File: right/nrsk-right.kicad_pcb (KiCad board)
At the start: 2 copper layers, 199.6 x 132.6 mm, 147 parts, among them J1 PJ-320D, J2 USB-C, J3 OLED 128x32, SW1 71, SW10 8, SW11 9, SW12 0, SW13 -, SW14 =, SW15 Backspace, SW16 75, SW17 Y, SW18 U, SW19 I, SW2 F7, SW20 O, SW21 P, SW22 [, SW23 ], SW24 \, SW25 77, SW26 H, SW27 J, SW28 K, SW29 L, SW3 F8, SW30 ;, SW31 ', SW32 Enter, SW33 79, SW34 N, SW35 M, SW36 ,, SW37 ., SW38 /, SW39 ↑, SW4 F9, SW40 fn, SW41 81, SW42 Space, SW43 Space, SW44 Cmd, SW45 Opt, SW46 ←, SW47 ↓, SW48 →, SW5 F10, SW6 F11, SW7 F12, SW8 73, SW9 7, U1 RP2040, U2 USBLC6-2SC6, U3 AS5600-ASOM, U4 AP2112K-3.3, U5 W25Q128JVS, Y1 12MHz

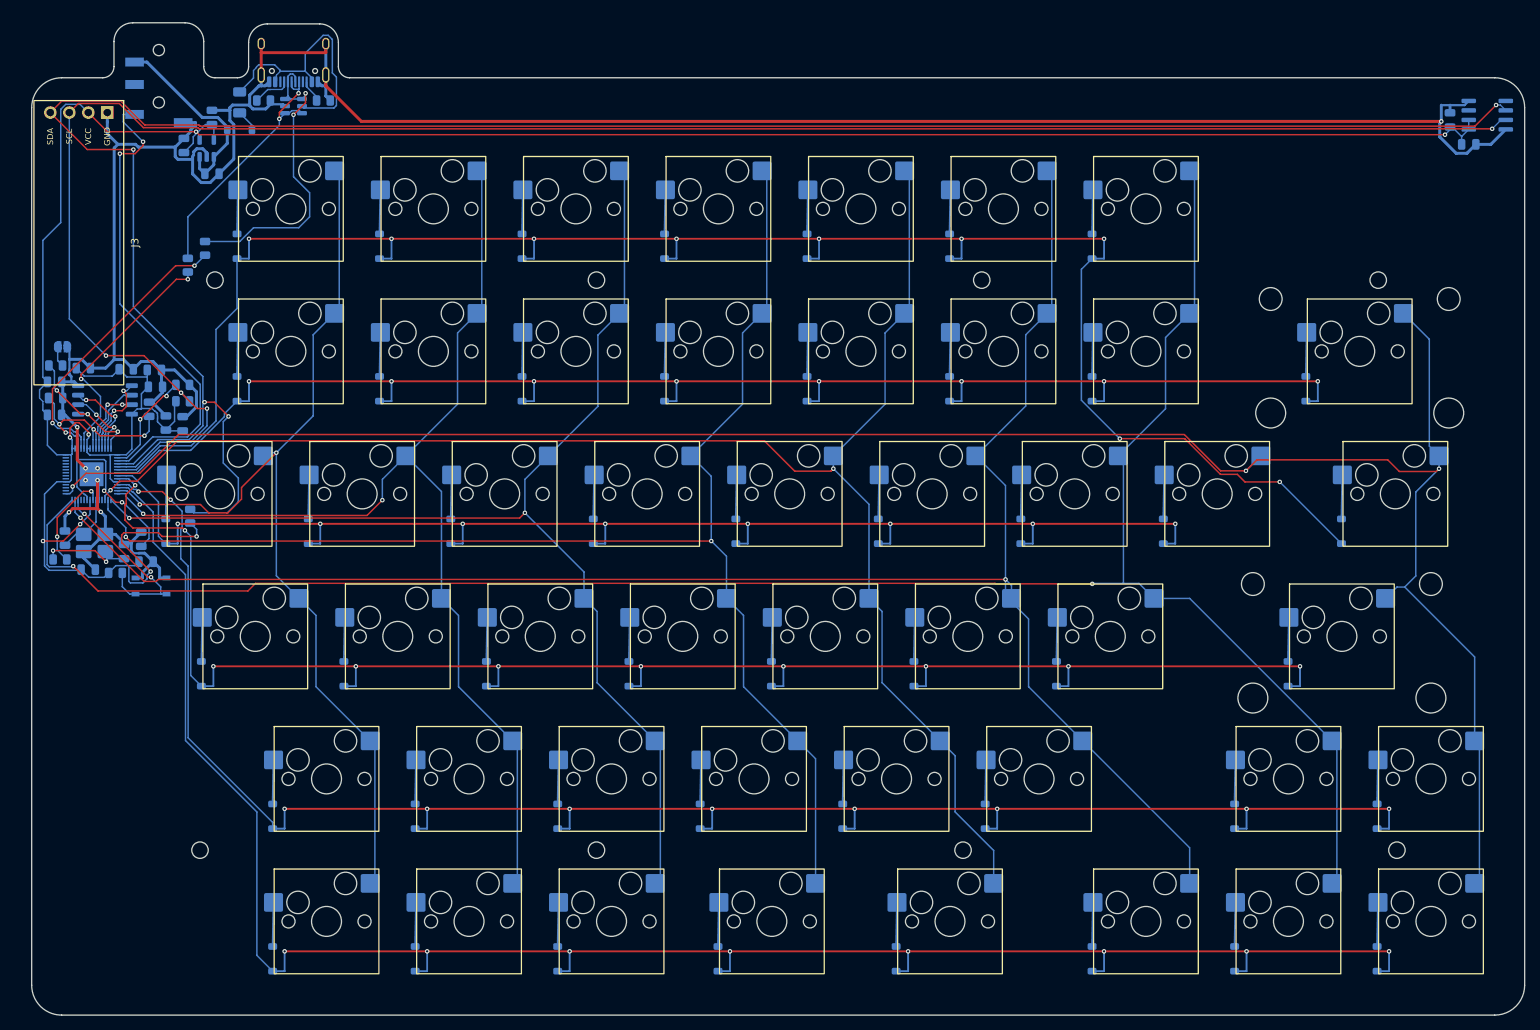
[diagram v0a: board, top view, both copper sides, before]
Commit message: PCB: thumbwheel encoder on the back at the wheel axis, boards re-routed (spec step 3) - ENC1 on the back, rotor on the wheel axis (where U3 was), terminals toward the board inside;   C9 / C10 gone from the support parts - The key turned 180 deg (socket below the stem) is now picked by geometry: a key whose   socket courtyard comes within 0.5 mm of the encoder courtyard. Left: Esc (SW1); right: none - Footprint Datasheet field left empty like the others (it differed from the symbol's) - Re-routed both halves; fab outputs regenerated - Checked: 0 unconnected, 0 DRC errors, 0 footprint errors, 0 schematic parity issues on   both halves (warnings: 5 silk-to-edge on J1/J2 as before, 3 / 2 dangling GND vias);   the gerber Edge.Cuts carries the rotor cut-out (3.1 mm square, lobes to +/-2.3 mm) at both wheel axes
Co-Authored-By: Claude Opus 5.5 <noreply@anthropic.com>
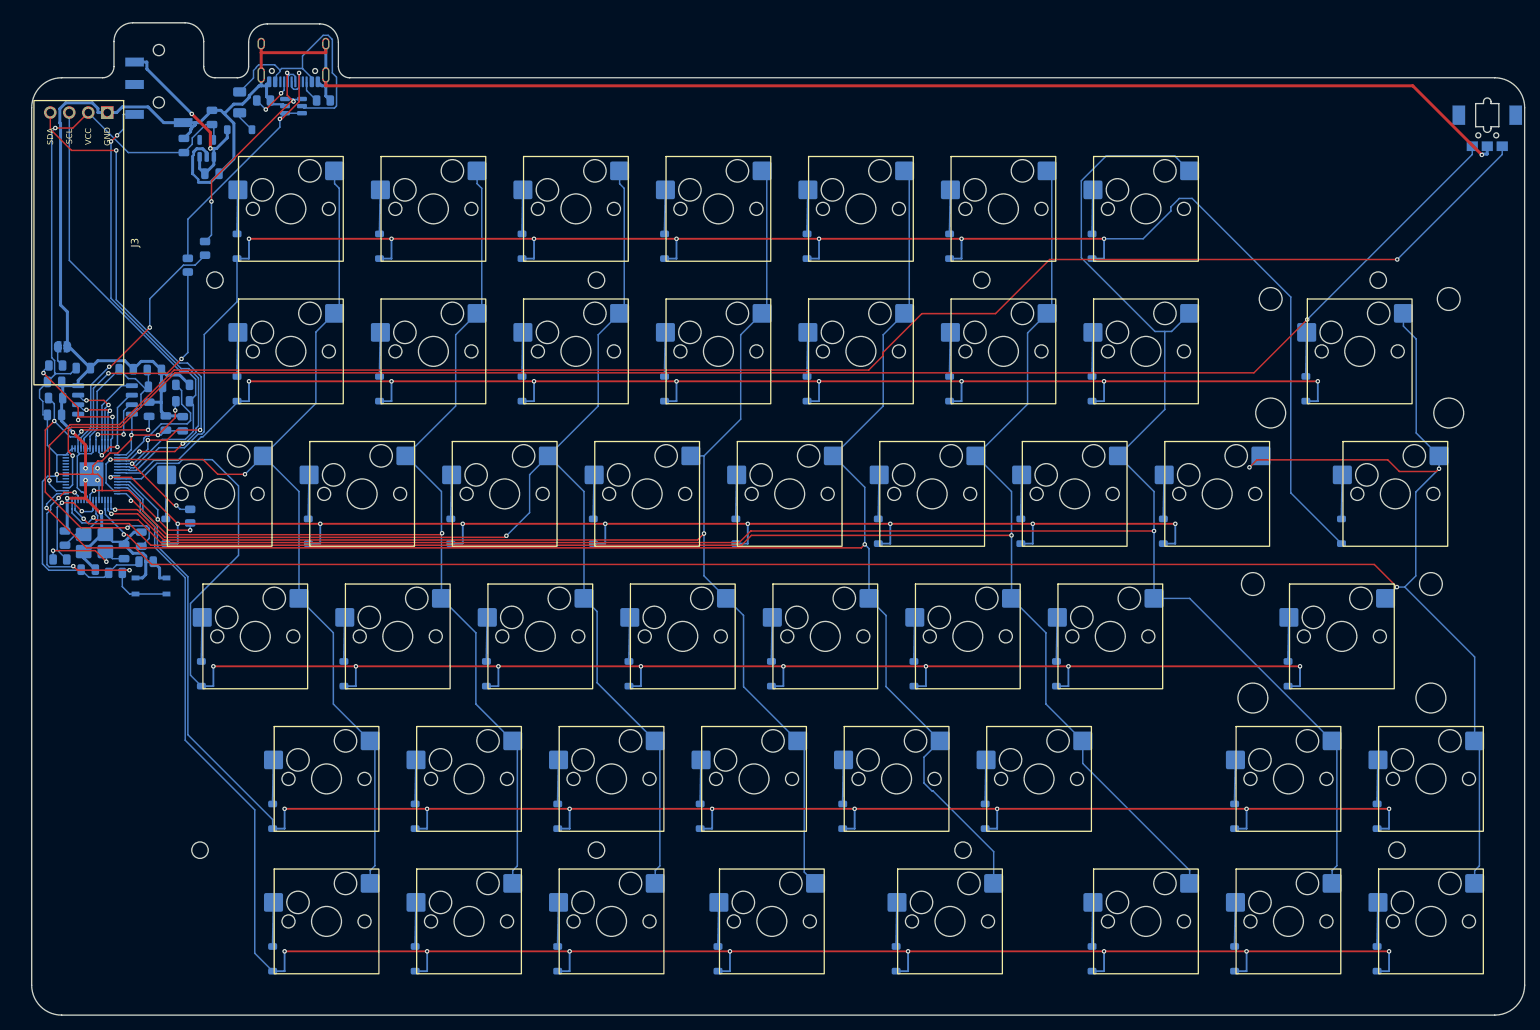
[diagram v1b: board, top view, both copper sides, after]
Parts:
- removed C10: 0.1uF, Capacitor_SMD:C_0805_2012Metric
- removed C9: 1uF, Capacitor_SMD:C_0805_2012Metric
- removed U3: AS5600-ASOM, Package_SO:SOIC-8_3.9x4.9mm_P1.27mm
- added ENC1: EC05E1220401, nrsk:Alps_EC05E1220401, B.Cu at (221.6, 27.0)
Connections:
- U1 pad 30: unconnected-(U1-GPIO19-Pad30) -> /ENC_A
- U1 pad 31: unconnected-(U1-GPIO20-Pad31) -> /ENC_B
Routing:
- net /ENC_A: track 0.00 -> 219.4 mm, vias 0 -> 2
- net /ENC_B: track 0.00 -> 212.7 mm, vias 0 -> 2
- net /SDA: track 289.6 -> 78.9 mm, vias 4 -> 5
- net /SCL: track 263.6 -> 63.0 mm, vias 4 -> 0
- net /3V3: track 375.2 -> 198.9 mm
- net /COL7: track 281.1 -> 304.9 mm, vias 3 -> 4
- net /COL6: track 272.0 -> 287.3 mm
- net GND: track 384.9 -> 374.1 mm
- net /ROW3: track 217.6 -> 228.0 mm, vias 10 -> 8
- net /COL2: track 165.4 -> 174.9 mm
- net /RUN: track 25.7 -> 33.9 mm, vias 2 -> 4
- net /USB_D-: track 41.6 -> 33.6 mm, vias 2 -> 3
- net /1V1: track 53.1 -> 59.8 mm, vias 6 -> 4
- net /ROW0: track 245.1 -> 251.6 mm, vias 9 -> 7
- net /D-: track 38.5 -> 33.7 mm
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
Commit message: Board top edge +1 mm so the left Esc switch is no longer turned 180 deg
- TOP = MARGIN + 6.0 (was + 5.0), both halves, so they stay the same height. The wheel is
  placed from the corner, so it and its encoder move up 1 mm with the edge
- The Esc socket overlapped the encoder keep-out by 0.43 mm; it now clears it by 0.575 mm
  (1.075 mm between courtyards), so on_encoder() finds no key and every switch faces north.
  Checked on the generated boards: 0 of 44 / 48 switch footprints rotated (was 1 on the left)
- Board 172.6 / 199.6 x 126.3 mm, case 189.6 / 216.6 x 143.3 mm (each 1 mm taller)
- ./build.sh rerun: boards rerouted (0 unconnected), DRC 8 per side (5 silk at the connector
  mouths, 3 GND thermal vias), the same kinds as before; case checks pass; case, laser files,
  BOM, JLC files, assembly guide, 3D viewer and doc images regenerated. The left side was
  routed again once to drop a 1.2 mm dangling stub on D-
- README: sizes, the Esc note (all switches now face the same way); spec: note on the outcome
- Not rerun: the Blender renders (render_all.sh); they differ only by the 1 mm

Co-Authored-By: Claude Opus 5.5 <noreply@anthropic.com>
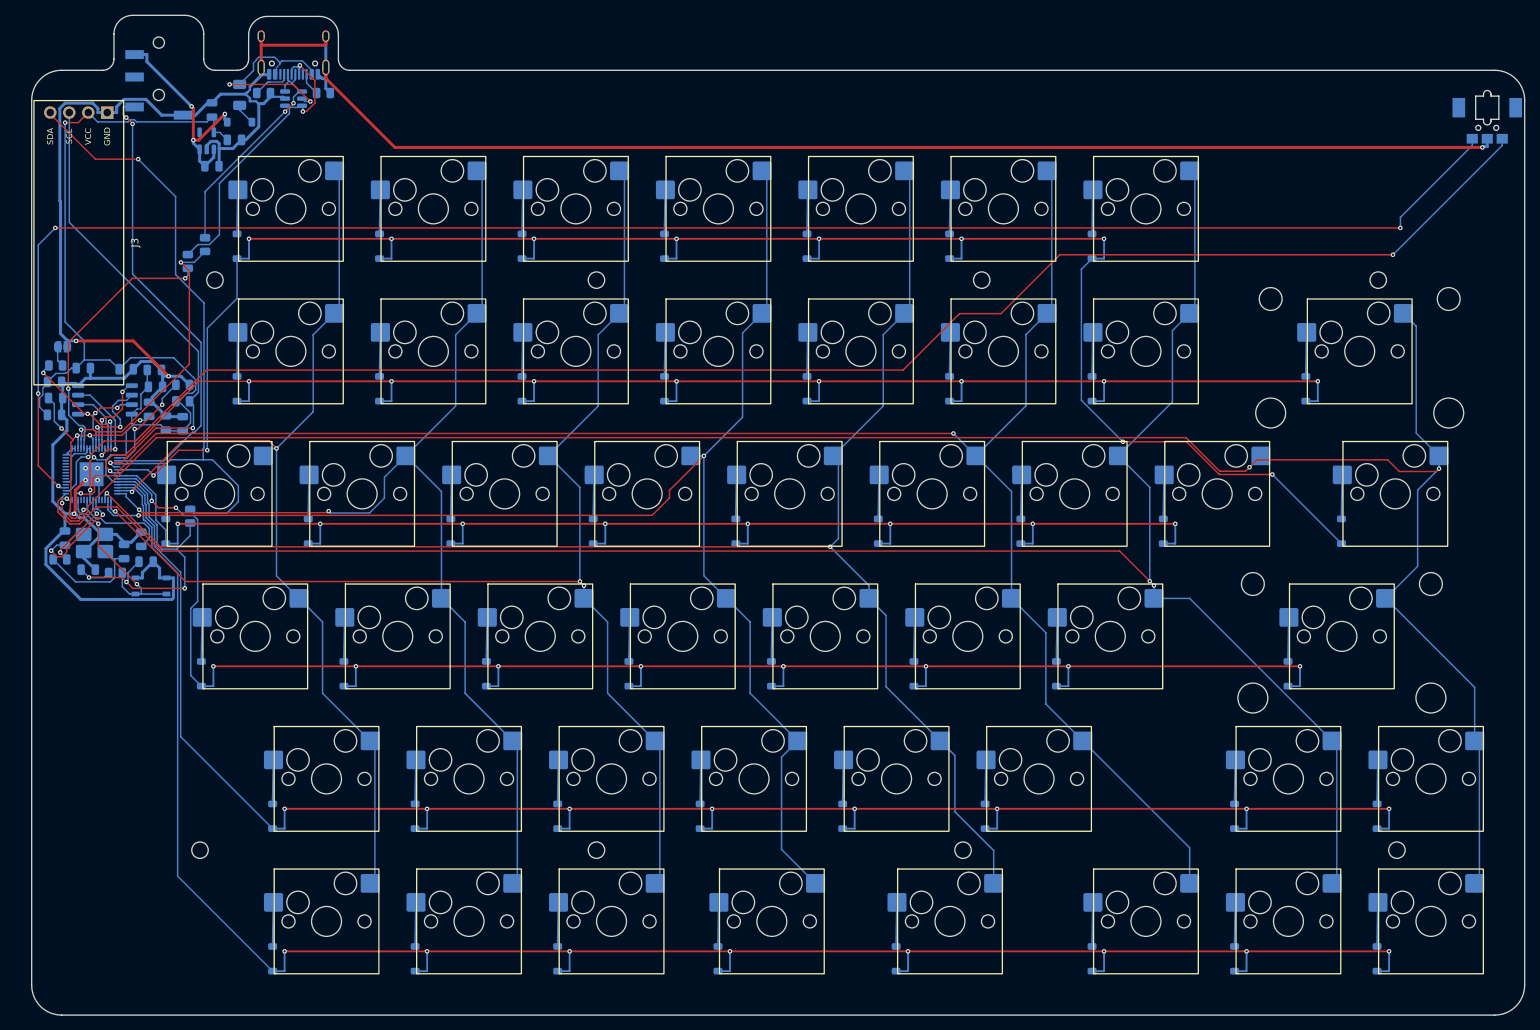
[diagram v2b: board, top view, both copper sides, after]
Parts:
- moved C19 6.05 mm to (51.1, 26.3)
- moved C17 4.24 mm to (54.1, 30.3), turned to 0 degrees
- moved C16 1.00 mm to (51.1, 33.8)
- moved D99 1.00 mm to (54.8, 27.9)
- moved ENC1 1.00 mm to (221.6, 26.0)
- moved F1 1.00 mm to (54.8, 24.3)
- moved J1 1.00 mm to (44.0, 22.1)
- moved J2 1.00 mm to (62.0, 17.5)
- moved R4 1.00 mm to (58.0, 24.0)
- moved R5 1.00 mm to (66.0, 24.0)
- moved U2 1.00 mm to (62.0, 24.8)
- moved U4 1.00 mm to (50.4, 30.4)
- moved R2 0.50 mm to (47.9, 46.6)
- moved R3 0.50 mm to (50.2, 44.3)
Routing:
- net GND: track 374.1 -> 408.9 mm
- net /ENC_B: track 212.7 -> 233.4 mm, vias 2 -> 4
- net /COL7: track 304.9 -> 284.3 mm, vias 4 -> 3
- net /COL6: track 287.3 -> 270.1 mm, vias 2 -> 3
- net /ROW3: track 228.0 -> 216.0 mm, vias 8 -> 10
- net /3V3: track 198.9 -> 188.2 mm, vias 8 -> 6
- net /1V1: track 59.8 -> 49.1 mm, vias 4 -> 5
- net /RUN: track 33.9 -> 24.8 mm, vias 4 -> 2
- net /XIN: track 8.56 -> 17.6 mm, vias 0 -> 2
- net /VBUS: track 36.0 -> 29.4 mm, vias 0 -> 2
- net /SDA: track 78.9 -> 85.6 mm, vias 5 -> 1
- net /ROW1: track 197.0 -> 203.0 mm, vias 8 -> 9
- net /COL4: track 216.1 -> 210.2 mm
- net /ENC_A: track 219.4 -> 213.7 mm
- net /D-: track 33.7 -> 38.8 mm
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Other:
- board size 199.6 x 132.6 mm -> 199.6 x 133.6 mm

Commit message: Right OLED turned like the left (header down); OLED pins fixed in the README
- The right OLED sat at 270 deg and the left at 90 deg, while the firmware uses one rotation
  (OLED_ROTATION_270) for both: one of the two displays would have been upside down. The right
  is now 90 deg too (header at the bottom); the module centre, and so the cover and the case,
  stay where they were
- case_data.json carries the OLED rotation; render_blender.py draws the glass from it instead of
  assuming the header end by side
- The MCU parts stay where they were placed by their pins. Mirroring the left cluster onto the
  right was tried: the right sockets are not mirrored and one (SW16) takes the room of the
  crystal group, and the RP2040 can only be turned, not mirrored, so the mirrored flash ended up
  at the far end of the QSPI pin row and the right board would not route (5-6 nets open, 3 tries)
- Boards: left routed again (placement unchanged), right re-placed and routed; both 0 unconnected,
  DRC 8 each (5 silk at the connector mouths, 3 GND thermal vias), 0 parity issues, ERC 0.
  Case, laser files, 3D viewer, assembly guide, BOM, JLC files and doc images regenerated
- JLC CPL checked pad by pad: each LCSC part's EasyEDA footprint placed as the CPL says lands on
  the same-numbered KiCad pads within 0.2 mm (21 part types, both halves; reset switch, TRRS and
  USB-C checked by position)
- Renders: render_all.sh (1600 px, 160 samples) and render_compare.sh
- README: OLED on GP3 (SCL) / GP2 (SDA) (it still said PD0 / PD1 from the Pro Micro days); both
  modules face the same way. docs/thumbwheel-check.md: check the text orientation, and how to
  flip it in make_qmk.py if it is upside down

Co-Authored-By: Claude Opus 5.5 <noreply@anthropic.com>
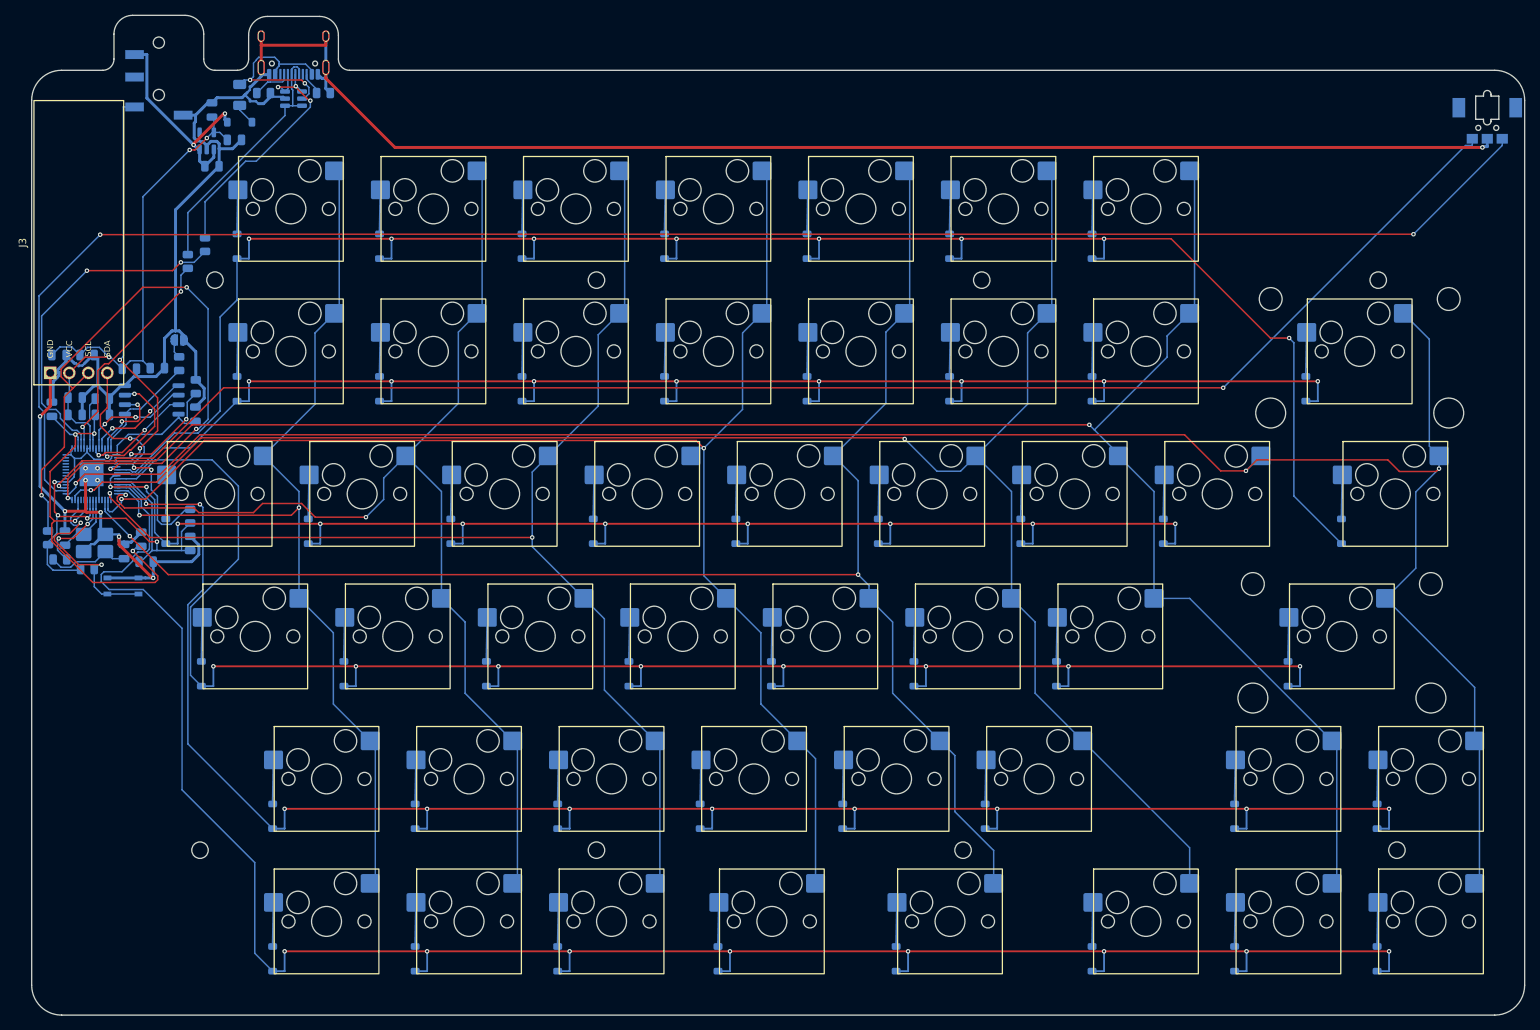
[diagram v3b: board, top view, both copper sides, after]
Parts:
- moved R8 25.6 mm to (29.2, 83.5), turned to 90 degrees
- moved C12 23.1 mm to (32.8, 64.8)
- moved R7 16.5 mm to (46.7, 60.2), turned to 90 degrees
- moved C8 16.0 mm to (48.2, 84.2)
- moved JP1 15.6 mm to (46.7, 57.1)
- moved C6 13.0 mm to (29.7, 66.3)
- moved C20 11.0 mm to (48.9, 67.0), turned to 90 degrees
- moved C13 10.2 mm to (40.1, 60.9)
- moved C15 9.22 mm to (34.4, 59.1)
- moved C7 9.10 mm to (36.4, 64.9), turned to 0 degrees
- moved C4 6.64 mm to (36.5, 67.1)
- moved U5 6.25 mm to (43.0, 65.1)
- moved R6 3.78 mm to (34.5, 87.7)
- moved RSW1 3.75 mm to (39.2, 89.9)
- moved C18 3.69 mm to (30.6, 59.1)
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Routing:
- net /SDA: track 85.6 -> 35.0 mm, vias 1 -> 3
- net GND: track 408.9 -> 379.5 mm, vias 8 -> 10
- net /ENC_B: track 233.4 -> 209.9 mm, vias 4 -> 2
- net /3V3: track 188.2 -> 167.0 mm, vias 6 -> 7
- net /SCL: track 64.2 -> 84.3 mm, vias 2 -> 4
- net /ENC_A: track 213.7 -> 233.2 mm
- net /ROW3: track 216.0 -> 227.9 mm, vias 10 -> 8
- net /1V1: track 49.1 -> 58.9 mm, vias 5 -> 4
- net /ROW5: track 256.2 -> 265.9 mm
- net /XIN: track 17.6 -> 8.38 mm, vias 2 -> 0
- net /COL6: track 270.1 -> 261.3 mm, vias 3 -> 2
- net /D-: track 38.8 -> 46.3 mm
- net /DATA: track 61.6 -> 54.4 mm
- net /USB_D+: track 40.6 -> 34.5 mm, vias 2 -> 0
- net /ROW1: track 203.0 -> 197.1 mm, vias 9 -> 8
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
